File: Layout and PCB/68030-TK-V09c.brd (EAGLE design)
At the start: 92.9 x 100.2 mm, 65 parts, among them IC10 74HCT245DW, IC11 74HCT245DW, IC4 74HCT245DW, IC5 74HCT245DW, IC6 74HCT245DW, IC8 74HCT245DW, IC9 74HCT245DW, X1 FABC96R

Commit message: minor clean up
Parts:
- added R17: 4,7k, rcl:R0603
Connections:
- removed net RW_OUT: IC7.22, IC9.2
- new net AMIGA_ADR_ENABLE: IC4.19, IC7.33, IC8.19, IC9.19
- net A6: now also IC7.22; no longer IC7.42
- net AS_00: now also IC7.42; no longer IC7.33
- net AVEC: now also R17.2
- net GND: no longer IC4.19, IC8.19, IC9.19
- net R/W: now also IC9.2
- net VCC: now also R17.1
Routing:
- net AMIGA_ADR_ENABLE: track 0.00 -> 99.7 mm
- net RW_OUT: track 95.5 -> 0.00 mm, vias 2 -> 0
- net R/W: track 154.7 -> 174.9 mm, vias 4 -> 5
- net AVEC: track 103.7 -> 109.2 mm, vias 3 -> 4
- net GND: track 121.0 -> 116.4 mm, vias 163 -> 159
- net AS_00: track 112.0 -> 108.3 mm
- net A6: track 119.3 -> 116.5 mm
- net VCC: track 143.9 -> 145.3 mm

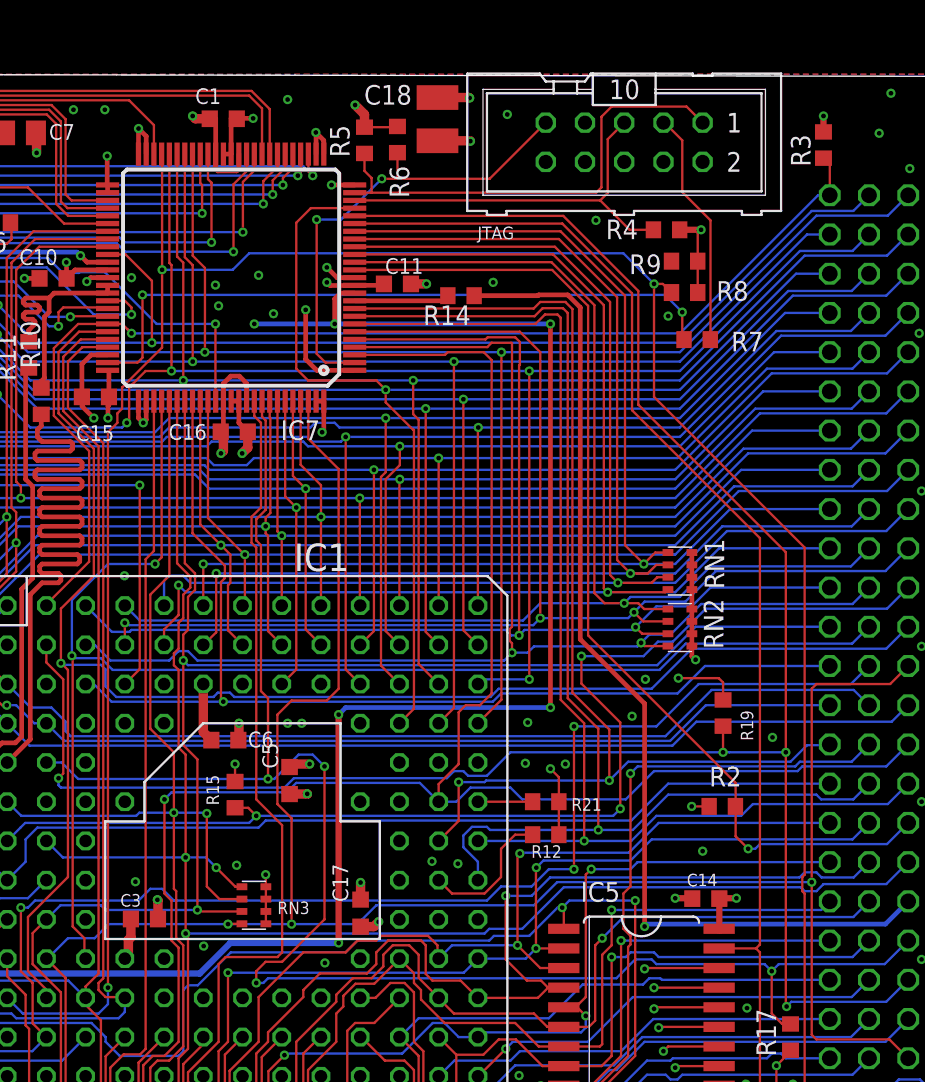
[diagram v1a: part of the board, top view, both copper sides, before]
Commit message: New PCB and start for RW-Signal-Optimization
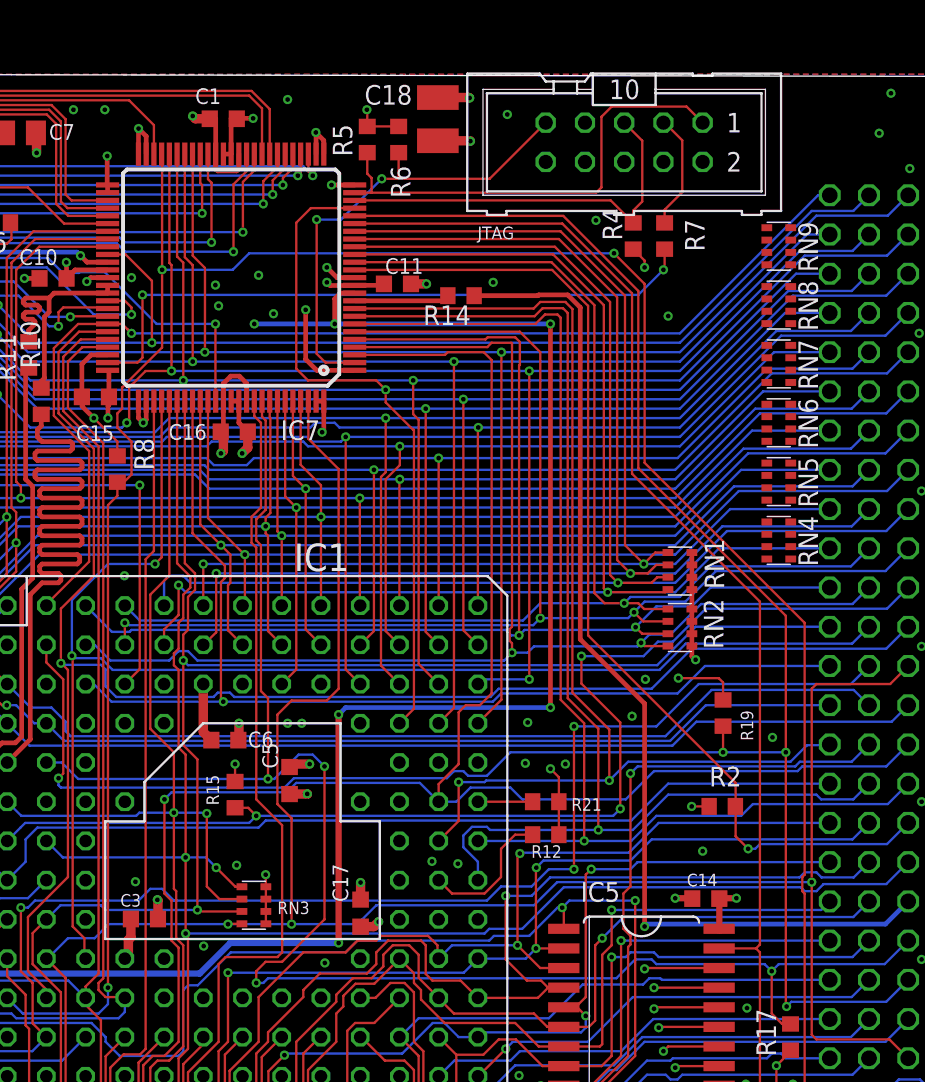
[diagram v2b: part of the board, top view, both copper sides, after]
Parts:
- removed R3, R9: 4,7k, rcl:R0603
- added RN4, RN5, RN6, RN7, RN8, RN9: 4,7k, resistor-dil:EXBV8V
- moved R8 38.5 mm to (36.4, 74.4), turned to 270 degrees
- moved R7 7.03 mm to (71.9, 89.5), turned to 270 degrees
- moved R4 2.20 mm to (69.8, 89.5), turned to 270 degrees
- moved R5 0.18 mm to (52.6, 95.8)
- moved R6 0.08 mm to (54.6, 95.8)
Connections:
- removed net RAM_SEL: IC7.14, R2.1, X1.A16
- net A0: now also RN9.1; no longer R3.1
- net A1: now also RN9.2
- net A10: now also RN7.3
- net A11: now also RN7.4
- net A12: now also RN6.1
- net A13: now also RN6.2
- net A14: now also RN6.3
- net A15: now also RN6.4
- net A16: now also RN5.1
- net A17: now also RN5.2
- net A18: now also RN5.3
- net A19: now also RN5.4
- net A2: now also RN9.3
- net A20: now also RN4.1
- net A21: now also RN4.2
- net A22: now also RN4.3
- net A23: now also RN4.4
- net A3: now also RN9.4
- net A4: now also RN8.1
- net A5: now also RN8.2
- net A6: now also RN8.3
- net A7: now also RN8.4
- net A8: now also RN7.1
- net A9: now also RN7.2
- net GND: now also RN4.5, RN4.6, RN4.7, RN4.8, RN5.5, RN5.6, RN5.7, RN5.8, RN6.5, RN6.6, RN6.7, RN6.8, RN7.5, RN7.6, RN7.7, RN7.8, RN8.5, RN8.6, RN8.7, RN8.8, RN9.5, RN9.6, RN9.7, RN9.8; no longer R3.2
- net IO_EXP: now also IC7.14, R2.1, X1.A16; no longer R9.2
- net VCC: no longer R9.1
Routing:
- net RAM_SEL: track 66.6 -> 0.00 mm, vias 1 -> 0
- net IO_EXP: track 0.00 -> 66.6 mm, vias 0 -> 1
- net TDO-PIN: track 15.4 -> 7.51 mm
- net A0: track 76.5 -> 74.0 mm
- net VCC: track 145.3 -> 143.5 mm
- net TDO: track 43.7 -> 42.2 mm
- net GND: track 116.4 -> 115.4 mm, vias 159 -> 158
- net CIIN: track 168.0 -> 167.3 mm
